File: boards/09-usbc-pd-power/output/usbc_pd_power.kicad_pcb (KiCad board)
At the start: 4 copper layers, 100 x 65 mm, 47 parts, among them J1 USB-C PD INPUT, J2 5V OUTPUT, J3 I2C HOST 3V3, Q1 AO4407A, Q2 AO4407A, U1 STUSB4500QTR, U2 TPS54302DDCR, U3 INA226AIDGSR, U4 TLV76033DBZR

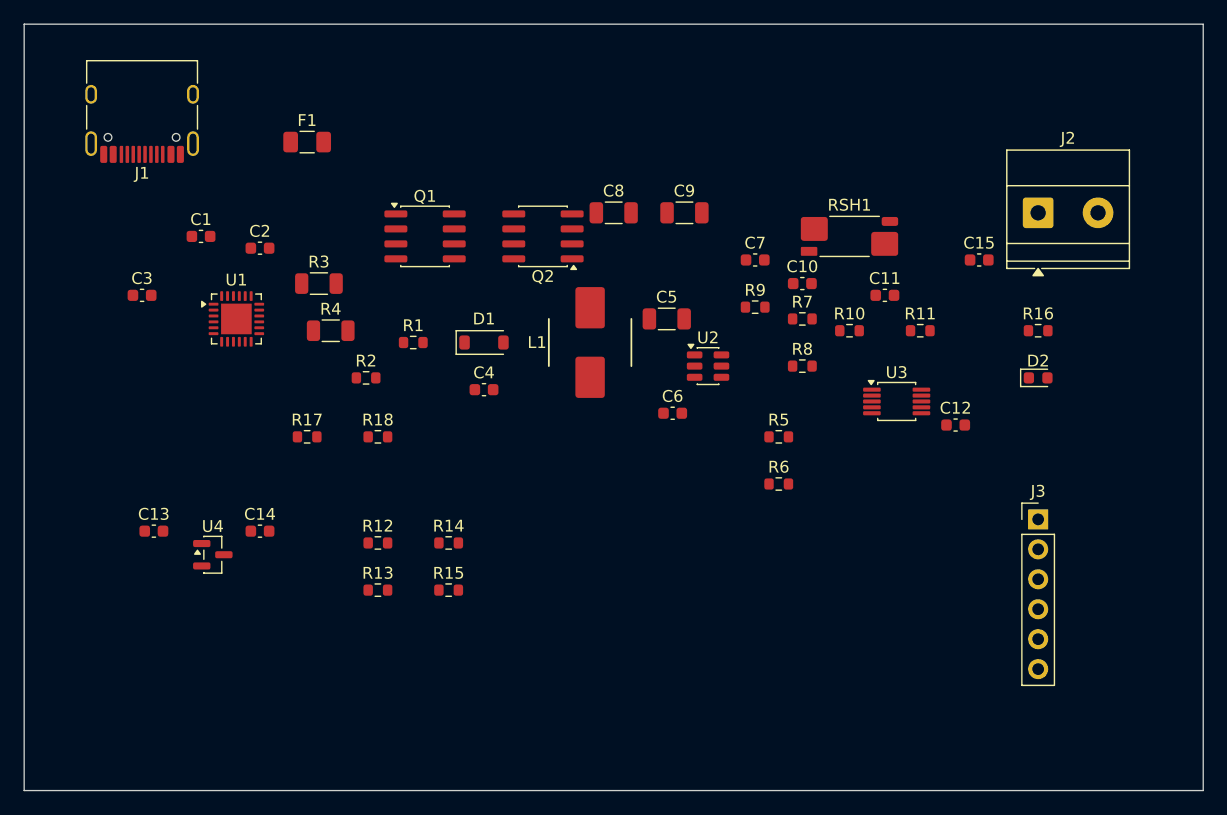
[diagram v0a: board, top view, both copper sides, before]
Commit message: feat(boards): route board09 critical connections and define board08 interface
Add explicit buck bypass and switch-node connections, isolated shunt sense routes, and native geometry checks with separate open counts. Refresh the blocked board09 checkpoint and previews. Select and verify the ADS131M04/Pico pin-package interface and nominal acquisition budget for board08.

Validation: 41 focused Python tests, native board09 ERC and geometry checks, 16 readiness hashes, board08 interface audit, 57 site tests and gallery build. Board09 still has 109 opens; neither new board is manufacturing-ready. Follow-up gallery metadata request: #5055.
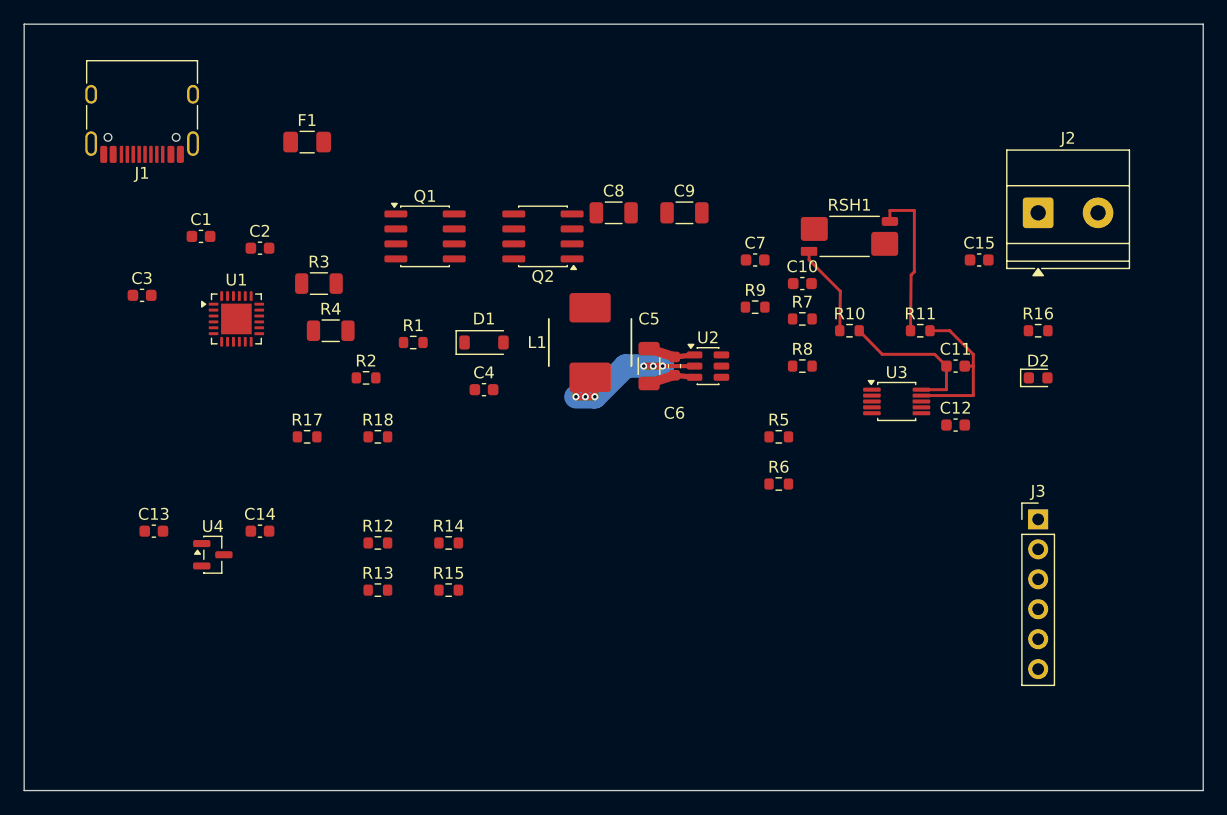
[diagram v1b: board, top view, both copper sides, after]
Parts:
- moved C11 8.49 mm to (177.5, 101.5)
- moved C5 4.27 mm to (151.5, 101.5), turned to 90 degrees
- moved C6 4.00 mm to (153.7, 101.5), turned to 90 degrees
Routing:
- net SW: track 0.00 -> 19.3 mm, vias 0 -> 6
- net KELVIN_N: track 0.00 -> 13.3 mm
- net SENSE_N: track 0.00 -> 13.1 mm
- net SENSE_P: track 0.00 -> 12.8 mm
- net KELVIN_P: track 0.00 -> 7.83 mm
- net VIN: track 0.00 -> 3.98 mm
- net GND: track 0.00 -> 3.98 mm
